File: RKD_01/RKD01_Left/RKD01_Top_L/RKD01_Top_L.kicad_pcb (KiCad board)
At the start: 2 copper layers, 176.2 x 126.2 mm, 41 parts, among them M1 Mark, M2 Mark, M3 Mark, M4 Mark, M5 Mark, SW1 SW_Push, SW10 SW_Push, SW11 SW_Push, SW12 SW_Push, SW13 SW_Push, SW14 SW_Push, SW15 SW_Push, SW16 SW_Push, SW17 SW_Push, SW18 SW_Push, SW19 SW_Push, SW2 SW_Push, SW20 SW_Push, SW21 SW_Push, SW22 SW_Push, SW23 SW_Push, SW24 SW_Push, SW25 SW_Push, SW26 SW_Push, SW27 SW_Push, SW28 SW_Push, SW29 SW_Push, SW3 SW_Push, SW30 SW_Push, SW31 SW_Push, SW32 SW_Push, SW33 SW_Push, SW34 SW_Push, SW4 SW_Push, SW5 SW_Push, SW6 SW_Push, SW66 SW_PUSH, SW7 SW_Push, SW8 SW_Push, SW9 SW_Push

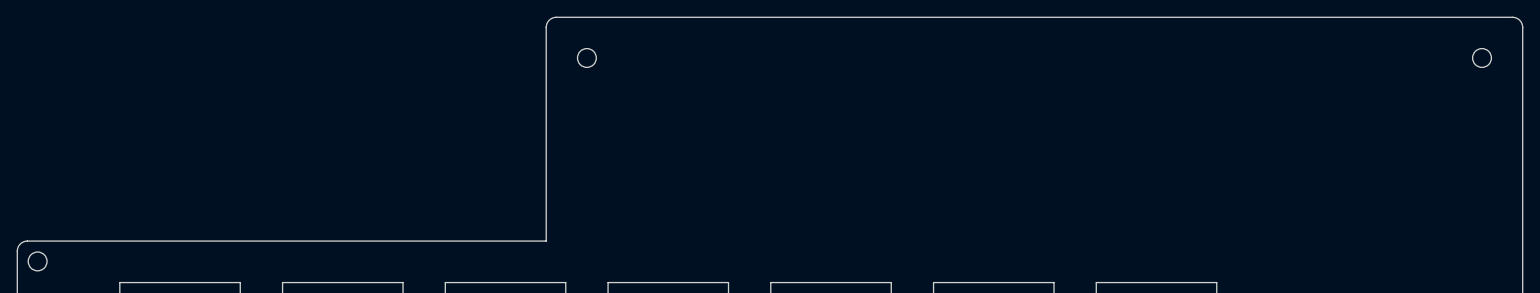
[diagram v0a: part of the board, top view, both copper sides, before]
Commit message: promicro部分拡張
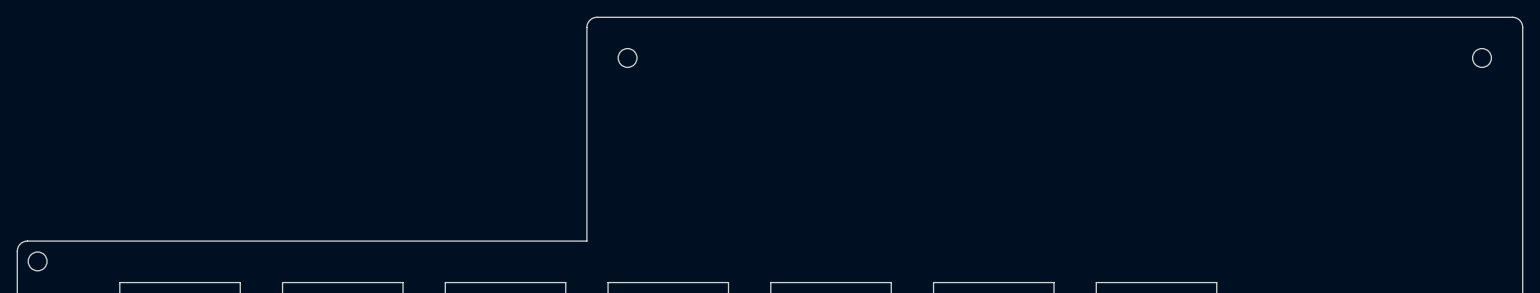
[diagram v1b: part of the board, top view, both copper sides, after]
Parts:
- moved M1 4.76 mm to (92.9, 23.8)
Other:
- outline, holes or cut-outs redrawn
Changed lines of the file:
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@@
 	(footprint "kbd_Hole:m2_Screw_Hole"
 		(layer "F.Cu")
-		(at 88.1063 23.8125)
+		(at 92.86875 23.8125)
 		(descr "Mounting Hole 2.2mm, no annular, M2")
 		(tags "mounting hole 2.2mm no annular m2")
@@
 	(gr_line
 		(start 22.62185 45.243725)
-		(end 83.34375 45.24375)
+		(end 88.106255 45.24375)
 		(stroke
 			(width 0.05)
@@
 	(gr_line
 		(start 196.453125 19.05)
-		(end 84.53437 19.049995)
+		(end 89.296845 19.049995)
 		(stroke
 			(width 0.05)
@@
 	)
 	(gr_arc
-		(start 83.343745 20.24062)
-		(mid 83.692472 19.398722)
-		(end 84.53437 19.049995)
+		(start 88.10622 20.24062)
+		(mid 88.454937 19.398697)
+		(end 89.296845 19.049995)
 		(stroke
 			(width 0.05)
@@
 	)
 	(gr_line
-		(start 83.34375 45.24375)
-		(end 83.343745 20.24062)
+		(start 88.106255 45.24375)
+		(end 88.10625 20.24062)
 		(stroke
 			(width 0.05)

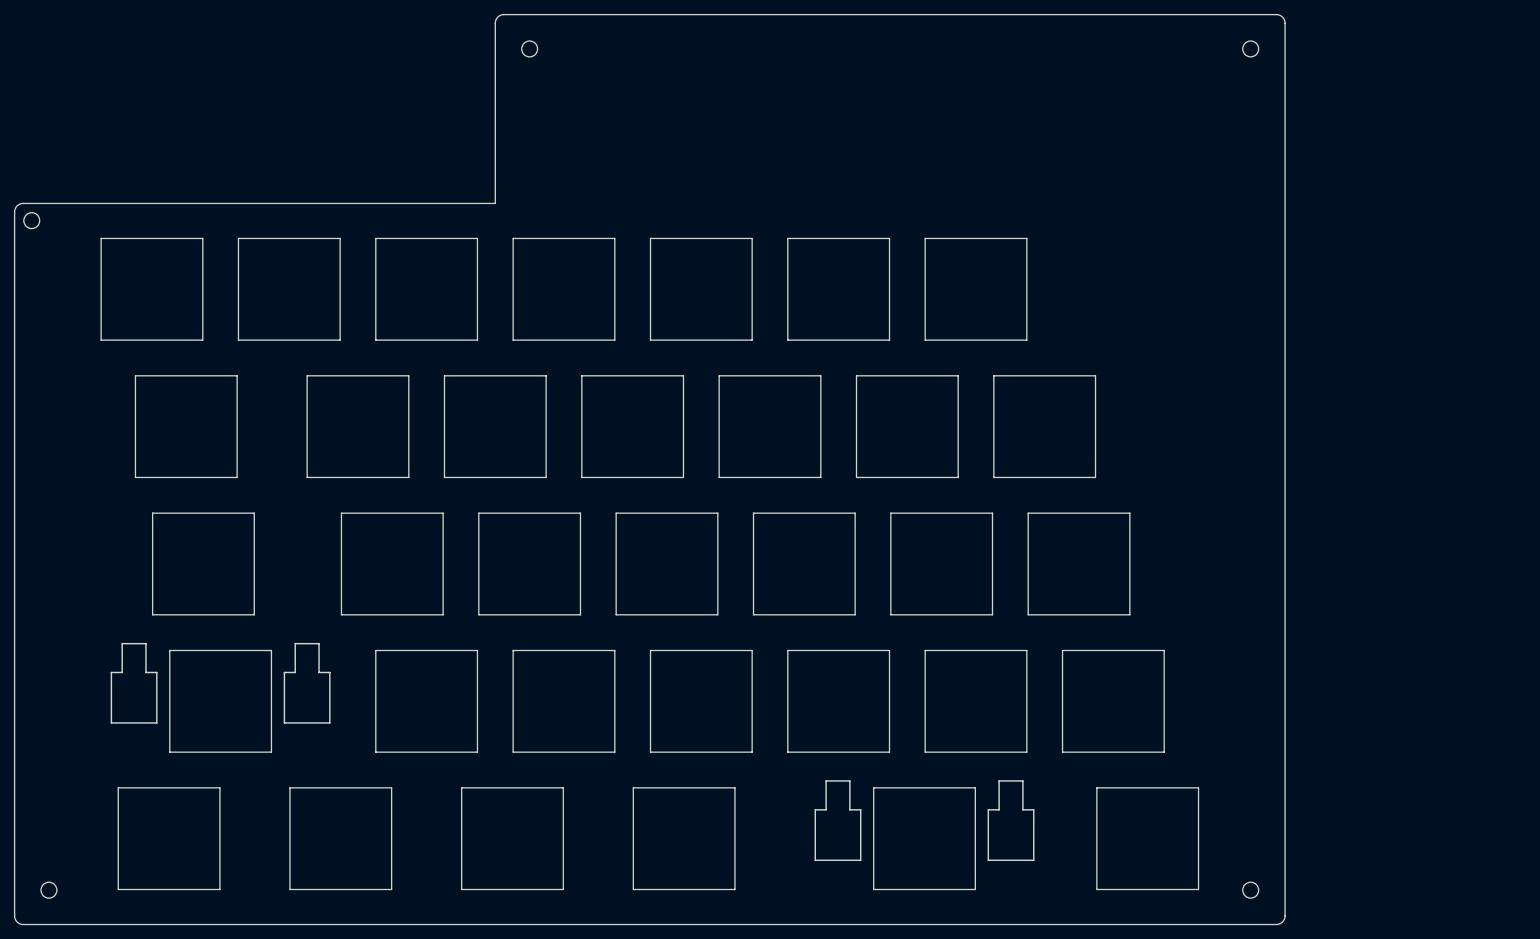
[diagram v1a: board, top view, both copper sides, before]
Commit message: 左一列追加Top
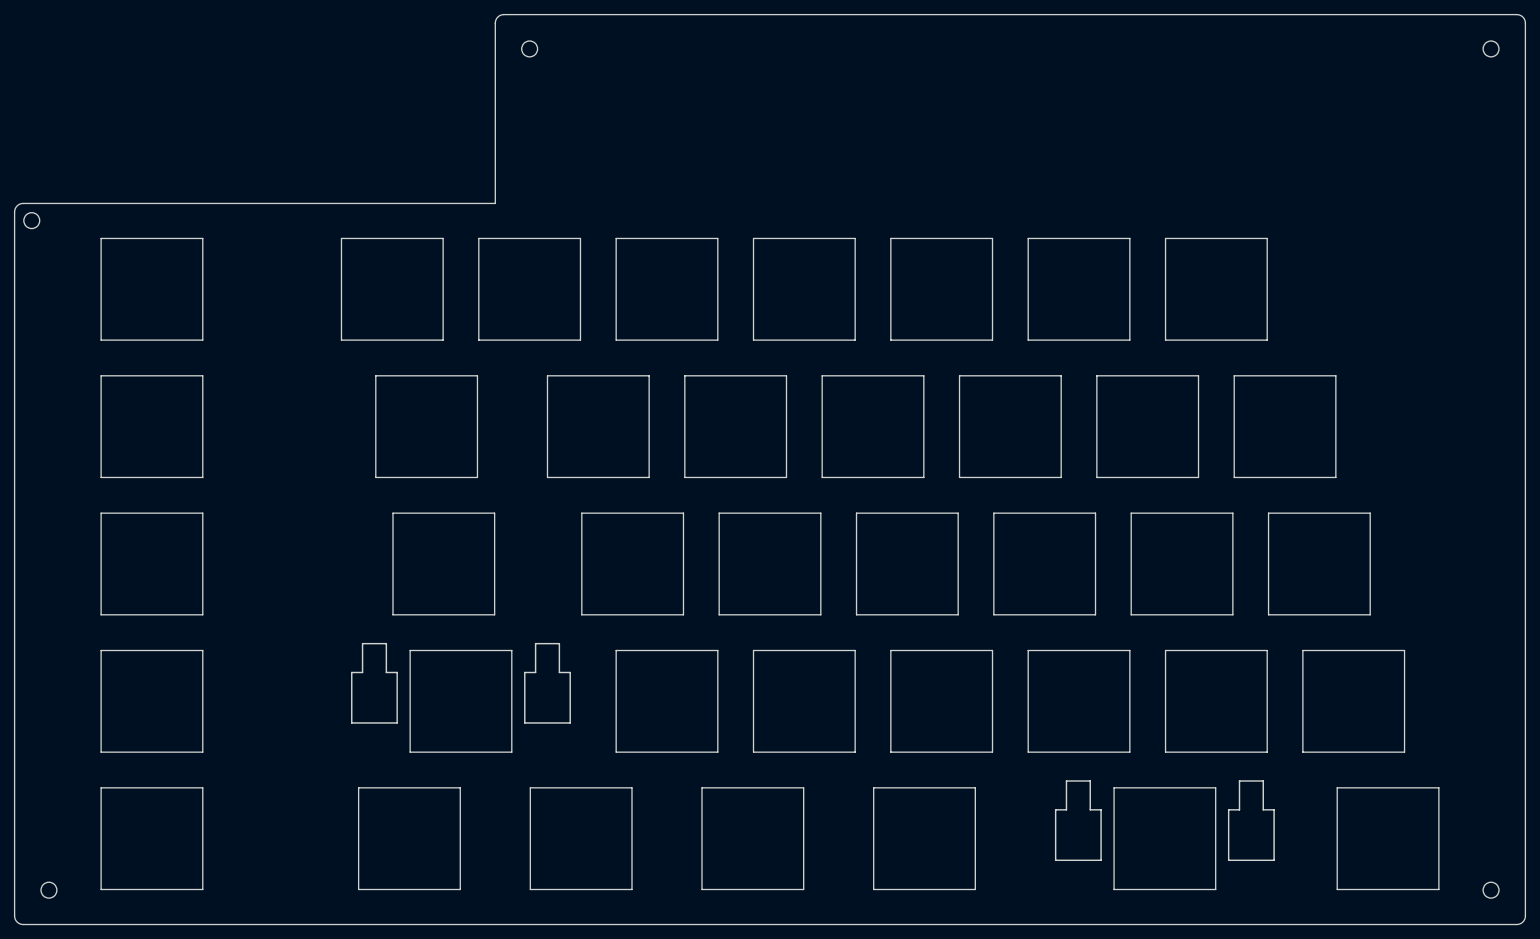
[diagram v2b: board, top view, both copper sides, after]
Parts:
- removed M5: Mark, kbd_Hole:m2_Screw_Hole
- removed the SW66 at (147.6, 133.3)
- removed the SW66 at (50.0, 114.3)
- added M6: Mark, kbd_Hole:m2_Screw_Hole, F.Cu at (23.8, 47.6)
- added SW1: SW_Push, kbd_SW_Hole:SW_Hole_1u, F.Cu at (40.5, 57.1)
- added SW2: SW_Push, kbd_SW_Hole:SW_Hole_1u, F.Cu at (40.5, 76.2)
- added SW3: SW_Push, kbd_SW_Hole:SW_Hole_1u, F.Cu at (40.5, 95.2)
- added SW4: SW_Push, kbd_SW_Hole:SW_Hole_1u, F.Cu at (40.5, 114.3)
- added SW5: SW_Push, kbd_SW_Hole:SW_Hole_1u, F.Cu at (40.5, 133.3)
- added SW66: SW_PUSH, kbd_SW_Hole:Stab_Hole_Choc_2u_Top, F.Cu at (83.3, 114.3)
- added SW66: SW_PUSH, kbd_SW_Hole:Stab_Hole_Choc_2u_Top, F.Cu at (181.0, 133.3)
- SW30: renamed from SW25; footprint kbd_SW_Hole:Stab_Hole_Choc_2u_Top -> kbd_SW_Hole:SW_Hole_1u
- SW9: renamed from SW4; footprint kbd_SW_Hole:Stab_Hole_Choc_2u_Top -> kbd_SW_Hole:SW_Hole_1u
- moved M2 33.3 mm to (226.2, 23.8)
- moved M4 33.3 mm to (226.2, 140.5)
- moved SW10 33.3 mm to (76.2, 133.3)
- moved SW12 33.3 mm to (102.4, 76.2)
- moved SW13 33.3 mm to (107.2, 95.2)
- moved SW14 33.3 mm to (111.9, 114.3)
- moved SW15 33.3 mm to (100.0, 133.3)
- moved SW16 33.3 mm to (111.9, 57.1)
- moved SW18 33.3 mm to (126.2, 95.2)
- moved SW20 33.3 mm to (123.8, 133.3)
- moved SW23 33.3 mm to (145.3, 95.2)
- moved SW24 33.3 mm to (150.0, 114.3)
- moved SW26 33.3 mm to (150.0, 57.1)
- moved SW27 33.3 mm to (159.5, 76.2)
- moved SW28 33.3 mm to (164.3, 95.2)
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- renumbered SW5 to SW10, SW6 to SW11, SW7 to SW12, SW8 to SW13, SW9 to SW14, SW10 to SW15, SW11 to SW16, SW12 to SW17, SW13 to SW18, SW14 to SW19, SW15 to SW20, SW16 to SW21, SW17 to SW22, SW18 to SW23, SW19 to SW24, SW20 to SW25, SW21 to SW26, SW22 to SW27, SW23 to SW28, SW24 to SW29, SW26 to SW31, SW27 to SW32, SW28 to SW33, SW29 to SW34, SW30 to SW35, SW31 to SW36, SW32 to SW37, SW33 to SW38, SW34 to SW39, SW1 to SW6, SW2 to SW7, SW3 to SW8
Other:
- board size 176.2 x 126.2 mm -> 209.6 x 126.2 mm

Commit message: 配置変更
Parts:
- removed M6: Mark, kbd_Hole:m2_Screw_Hole
- added M5: Mark, kbd_Hole:m2_Screw_Hole, F.Cu at (23.8, 47.6)
- added M7: Mark, kbd_Hole:m2_Screw_Hole, F.Cu at (178.6, 66.7)
- added M8: Mark, kbd_Hole:m2_Screw_Hole, F.Cu at (116.7, 104.8)
- SW10, SW15, SW20, SW25: footprint kbd_SW_Hole:SW_Hole_1.25u -> kbd_SW_Hole:SW_Hole_1u
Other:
- outline, holes or cut-outs redrawn
- board text added: "RKD01_Left v1.5"
- board text removed: "RKD01_Left v1.0"

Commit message: バージョン表記を修正
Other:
- board text added: "RKD01_Left v2"
- board text removed: "RKD01_Left v1.5"
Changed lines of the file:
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@@
 		(layer "Edge.Cuts")
 	)
-	(gr_text "RKD01_Left v1.5"
+	(gr_text "RKD01_Left v2"
 		(at 214.3125 23.8125 0)
 		(layer "B.SilkS")
